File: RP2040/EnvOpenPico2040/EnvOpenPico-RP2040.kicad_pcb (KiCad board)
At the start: 2 copper layers, 21 x 51 mm, 58 parts, among them J1 USB_C_Receptacle_USB2.0, J2 Button, J3 2.54mm header 01x20, J4 2.54mm header 01x20, J5 Conn_01x03_Male, Q1 SI2301B, U1 SOT-23-5 5.5V 3.3V 500mA, U3 RP2040, Y1 3225_4P 12MHz

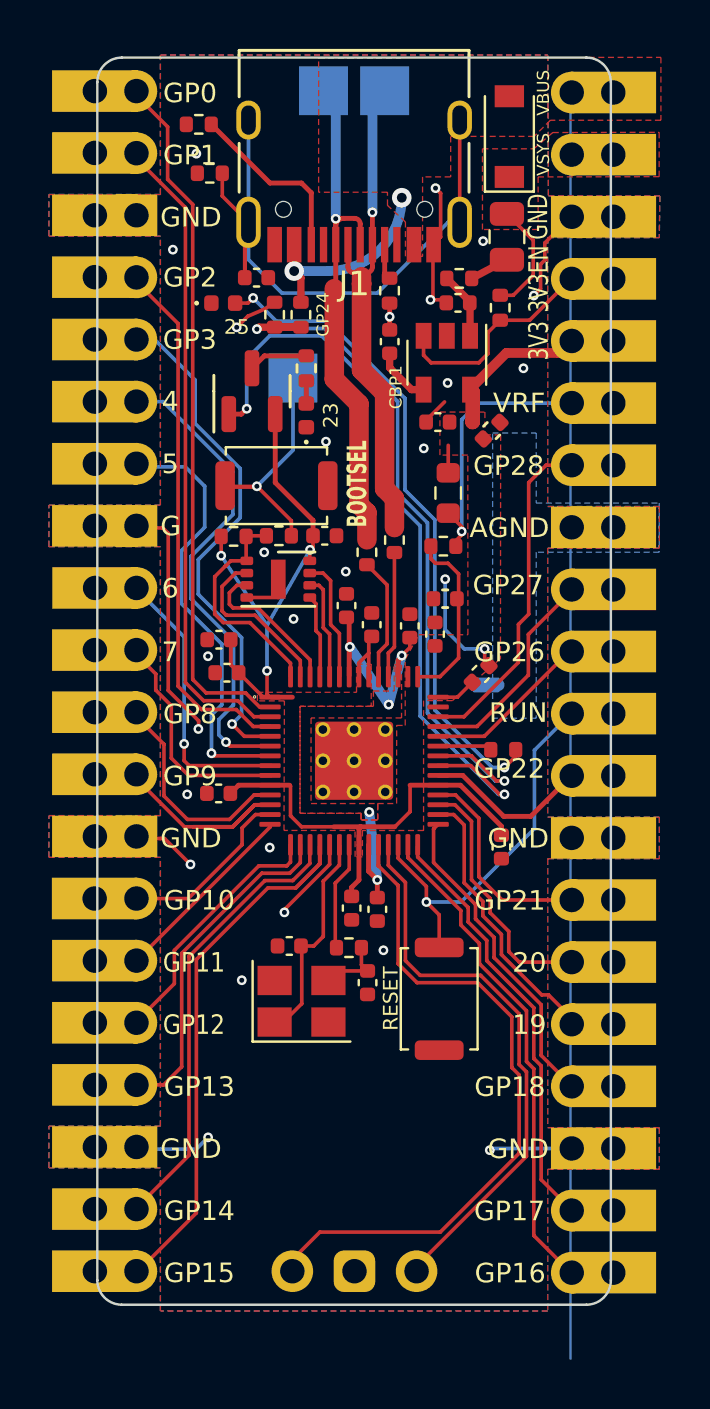
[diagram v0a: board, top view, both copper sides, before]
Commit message: made many corrections to RP2040 pico board, silkscreen, positioning, footprint, any errors I could find.
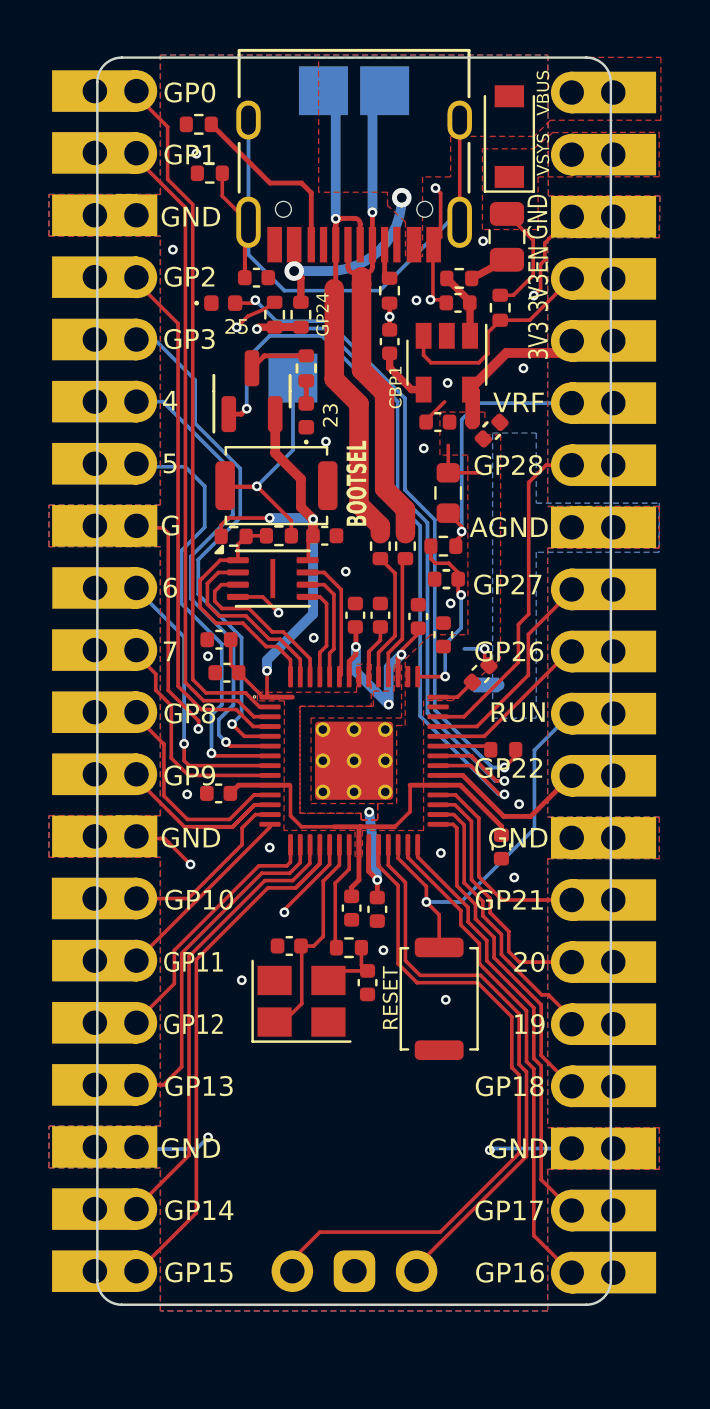
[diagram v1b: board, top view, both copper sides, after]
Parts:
- D1: value 1N4002W -> 1N5817W
- FLASH1: footprint Package_SON:SON-8-1EP_3x2mm_P0.5mm_EP1.4x1.6mm -> Package_SON:Winbond_USON-8-1EP_3x2mm_P0.5mm_EP0.2x1.6mm
- moved C102 0.80 mm to (107.4, 78.6)
- moved R3 0.60 mm to (104.7, 77.2)
- moved C7 0.53 mm to (103.7, 80.1)
- moved C8 0.52 mm to (104.7, 80.1)
- moved C3 0.52 mm to (106.3, 80.1)
- moved R4 0.51 mm to (105.8, 77.2)
- moved C10 0.34 mm to (107.3, 80.9)
- moved FLASH1 0.23 mm to (100.3, 78.6)
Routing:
- net +3V3: track 51.8 -> 55.2 mm
- net GND: track 43.5 -> 40.2 mm, vias 27 -> 32
- net /QSPI_SD2: track 6.24 -> 7.07 mm
- net /QSPI_SS: track 9.40 -> 10.2 mm
- net /QSPI_SD1: track 6.94 -> 7.73 mm
- net +1V1: track 14.1 -> 14.7 mm
- net /QSPI_SD0: track 3.40 -> 3.99 mm
- net Net-(U3-ADC_AVDD): track 7.34 -> 7.56 mm, vias 0 -> 2
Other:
- board text added: "#REV 1.5"
- board text added: "env"
- board text removed: "#REV 1.4"
